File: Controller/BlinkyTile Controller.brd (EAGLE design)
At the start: 40 x 25 mm, 27 parts, among them CON1 USB_MICROSMT+THRUHULE, CON2 F-2X05-DIL-100, Q1 CRYSTAL_4PAD2520, SW1 SPST_TACT-EVQQ2, SW2 SPST_TACT-EVQQ2, U1 MK20D--VFM5, U2 W25Q80BV, U3 74LVC1G17DCK, U4 74LVC1G17DCK, U5 74LVC1G17DCK

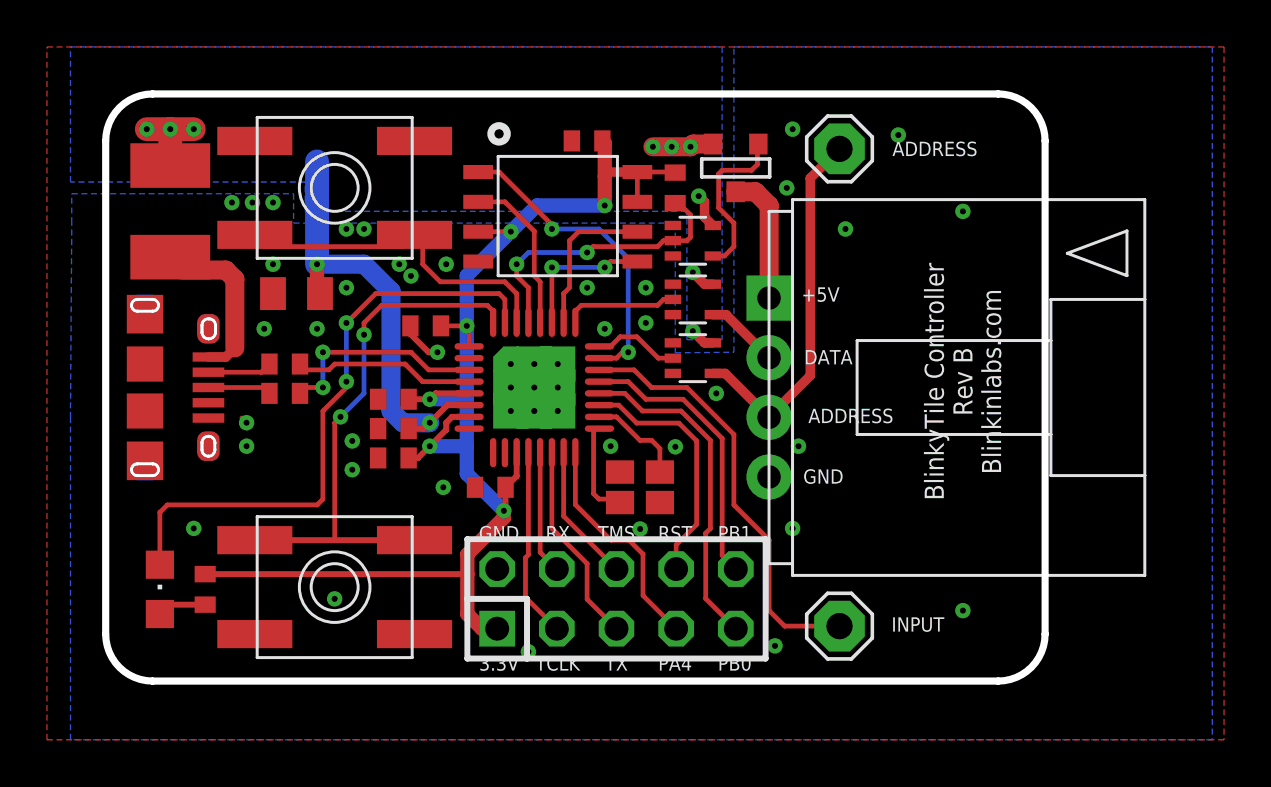
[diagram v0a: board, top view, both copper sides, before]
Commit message: Controller: Change .1" header footprint to Sparkfun version, make text larger
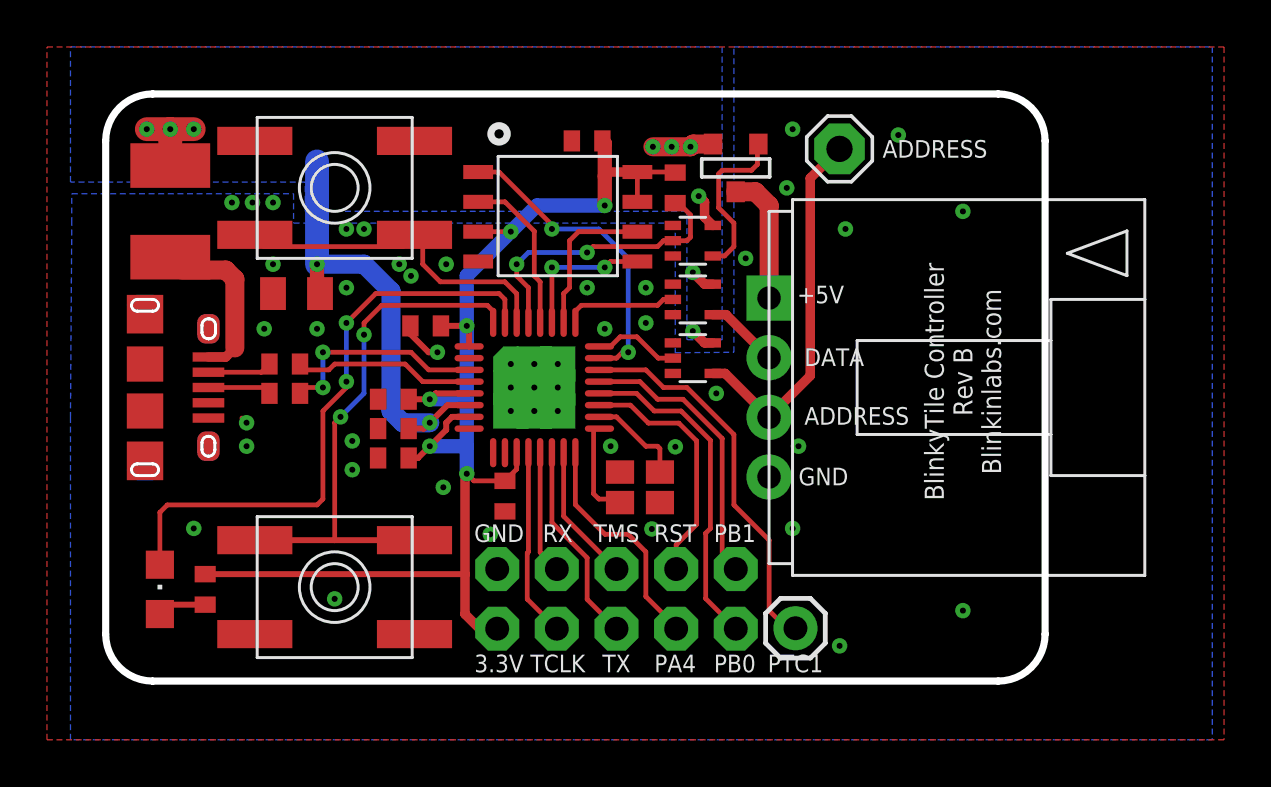
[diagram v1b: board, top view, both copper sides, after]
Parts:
- removed CON2: F-2X05-DIL-100, con-headers-jp:DIL-100-2X05
- removed TP1: ADCIN, solpad:SE11
- added JP1: M05X2NO_SILK, SparkFun-Connectors:2X5_NOSILK
- added JP3: M01PTH, SparkFun-Connectors:1X01
- moved C6 0.73 mm to (17.0, -4.62), turned to 270 degrees
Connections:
- net +3V3: now also JP1.1; no longer CON2.1
- net ADC15: now also JP3.1; no longer TP1.MP
- net GND: now also JP1.2; no longer CON2.2
- net PA4: now also JP1.7; no longer CON2.7
- net PB0: now also JP1.9; no longer CON2.9
- net PB1: now also JP1.10; no longer CON2.10
- net RESET: now also JP1.8; no longer CON2.8
- net RX: now also JP1.4; no longer CON2.4
- net TCLK: now also JP1.3; no longer CON2.3
- net TMS: now also JP1.6; no longer CON2.6
- net TX: now also JP1.5; no longer CON2.5
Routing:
- net ADC15: track 18.3 -> 16.4 mm
- net +3V3: track 58.3 -> 57.3 mm
- net GND: vias 38 -> 39
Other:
- board text added: "PTC1"
- board text removed: "INPUT"

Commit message: Controller: move end of 3.3v trace to improve grounding, replace switch, resize 5v line
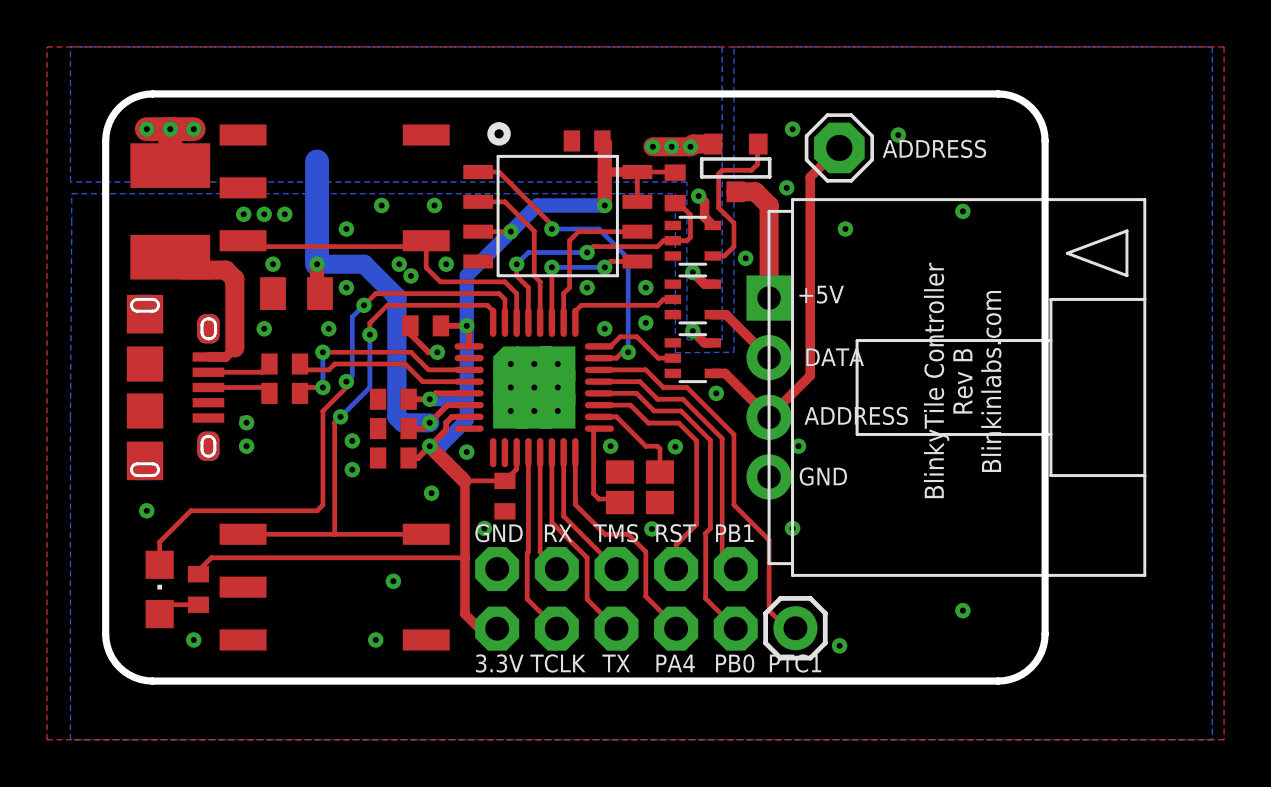
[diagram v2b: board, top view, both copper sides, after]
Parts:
- removed SW1, SW2: SPST_TACT-EVQQ2, adafruit:EVQ-Q2
- added U$1, U$2: BUTTON_MOMENTARY_GROUND, blinkinlabs:TD-07XB
- moved R4 0.29 mm to (3.95, -8.60)
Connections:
- net GND: now also U$1.1, U$1.2, U$1.5, U$2.3, U$2.4, U$2.5; no longer SW1.A, SW1.A', SW2.A, SW2.A'
- net SW1: now also U$1.3, U$1.4; no longer SW1.B, SW1.B'
- net SW2: now also U$2.1, U$2.2; no longer SW2.B, SW2.B'
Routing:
- net +3V3: track 57.3 -> 58.0 mm, vias 6 -> 5
- net N$16: track 2.47 -> 1.82 mm
- net SW1: track 23.0 -> 23.6 mm
- net STATUS: track 25.7 -> 25.1 mm
- net GND: vias 39 -> 43

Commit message: Change 4p output connector, push switches in a bit
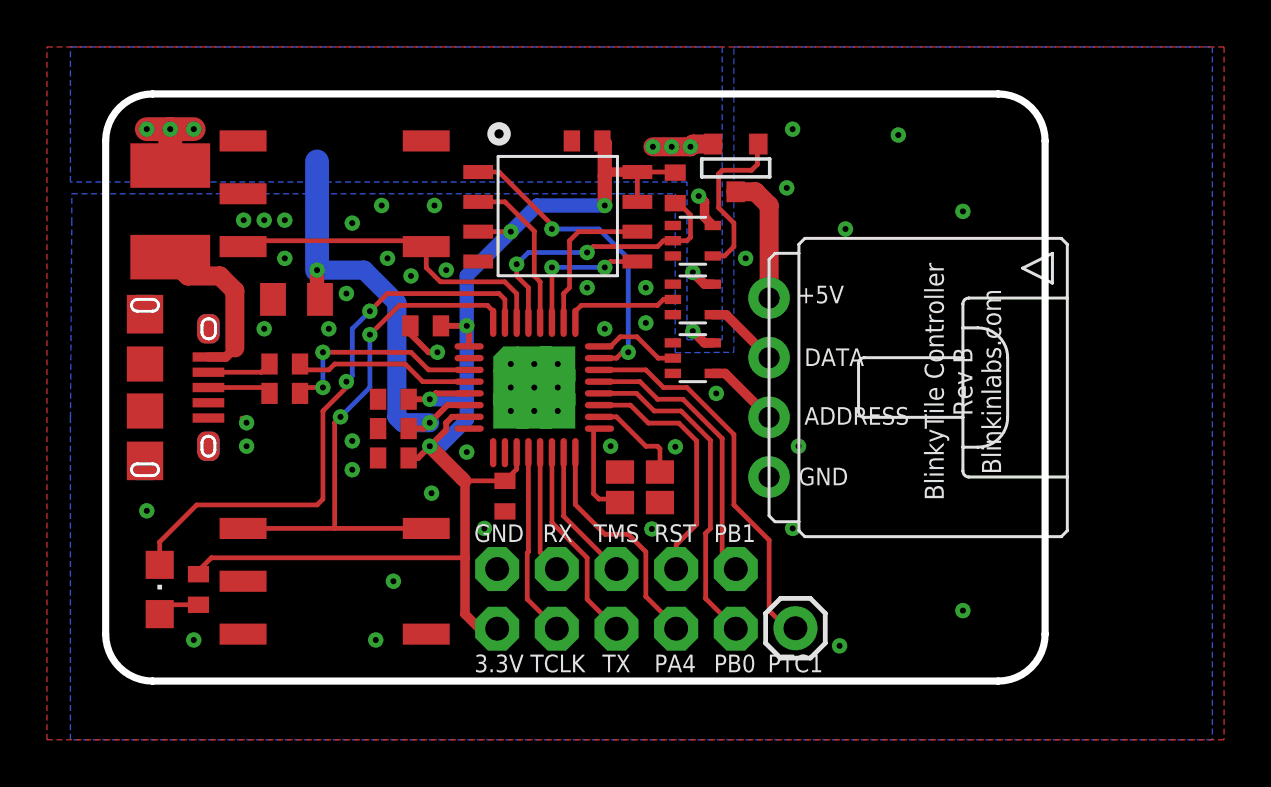
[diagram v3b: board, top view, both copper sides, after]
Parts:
- removed TP2: ADDRESS, solpad:SE11
- SV1: device dodocohedreled:4-PIN_DUPONT -> blinkinlabs:DUPONT-4P
- moved C8 0.25 mm to (8.12, 3.75)
- moved U$1 0.25 mm to (9.75, -8.25)
- moved U$2 0.25 mm to (9.75, 8.25)
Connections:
- net N$4: no longer TP2.MP
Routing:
- net N$4: track 15.9 -> 3.19 mm
- net SW1: track 23.6 -> 23.0 mm

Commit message: Update flash type, add .254mm isolation on top&bottom copper, general cleanup
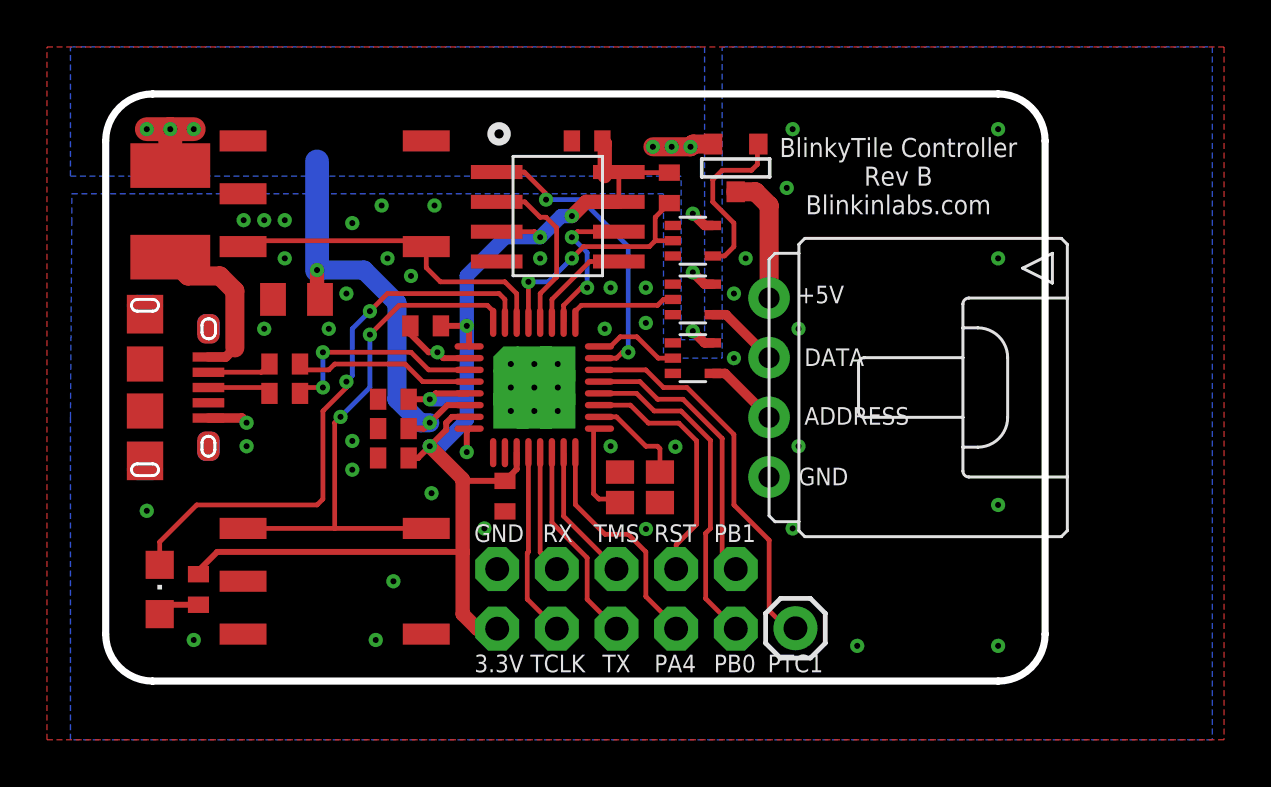
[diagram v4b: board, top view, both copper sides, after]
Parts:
- U2: value W25Q80BV -> W25Q80BV150; device Blinkin_Labs:SOIC8 -> blinkinlabs:SOIC8-150
- moved R5 0.25 mm to (24.0, 8.50)
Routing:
- net GND: track 2.10 -> 6.02 mm, vias 43 -> 45
- net POWER_ENABLE: track 12.6 -> 10.4 mm
- net FLASH_MOSI: track 6.08 -> 4.49 mm, vias 2 -> 0
- net +5V: track 29.0 -> 28.1 mm
- net FLASH_MISO: track 6.89 -> 7.67 mm
- net FLASH_SCK: track 6.63 -> 6.55 mm, vias 0 -> 2
